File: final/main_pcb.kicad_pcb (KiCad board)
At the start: 2 copper layers, 136.8 x 105.5 mm, 93 parts

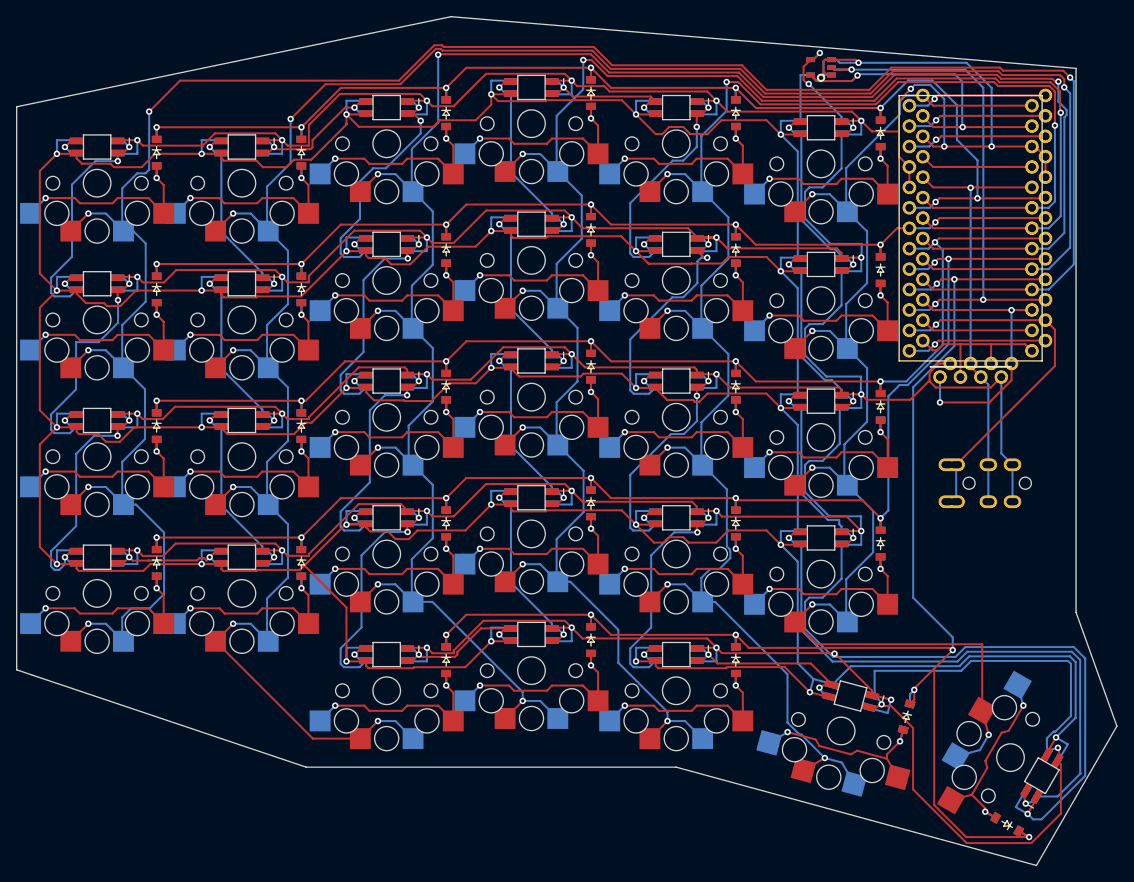
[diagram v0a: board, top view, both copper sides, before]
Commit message: Fix outline to have 0.3mm gap to traces
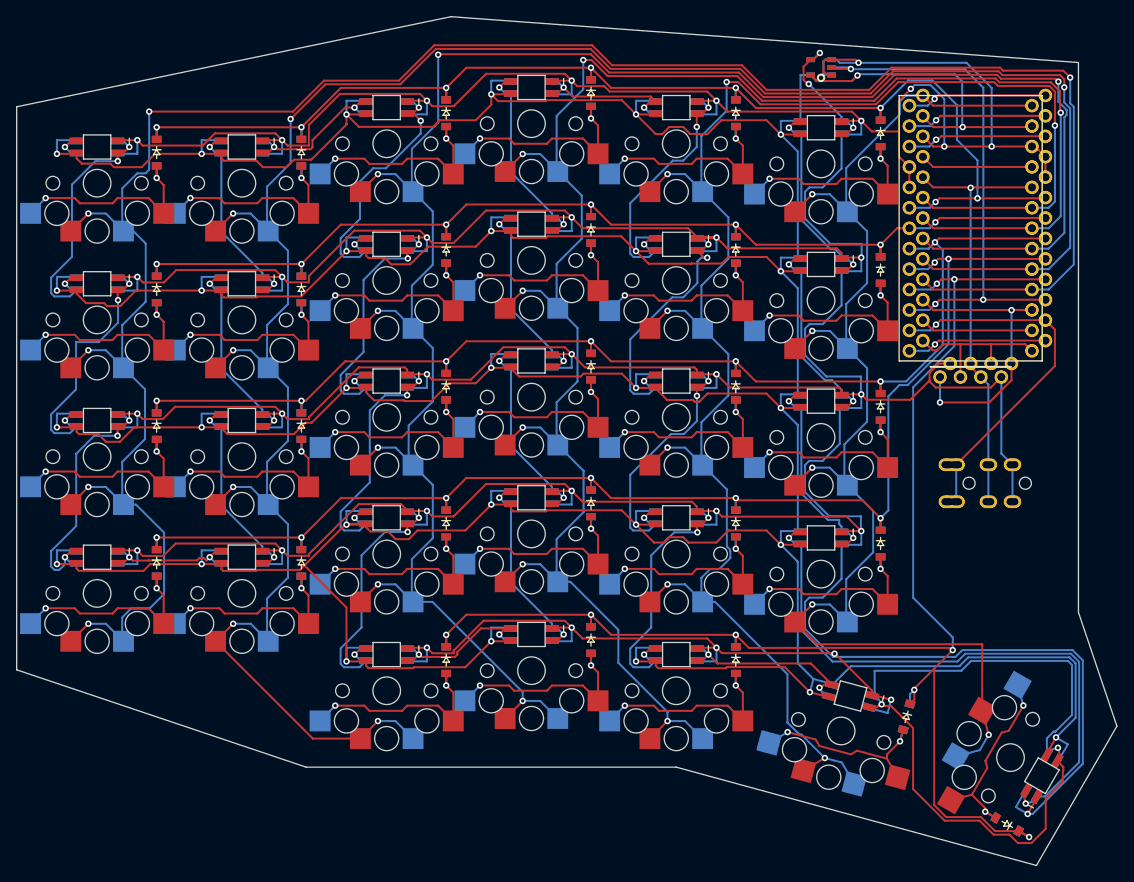
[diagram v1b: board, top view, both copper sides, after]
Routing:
- net RAW: track 837.6 -> 781.1 mm
- net GND: track 912.0 -> 909.6 mm
- net RMod: track 186.8 -> 185.2 mm
- net LED_4: track 75.8 -> 74.3 mm
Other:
- outline, holes or cut-outs redrawn

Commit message: Add picture footprnts and add to PCB Fix TRRS Power line on kicadpcb to 5v Add Readme on changes made
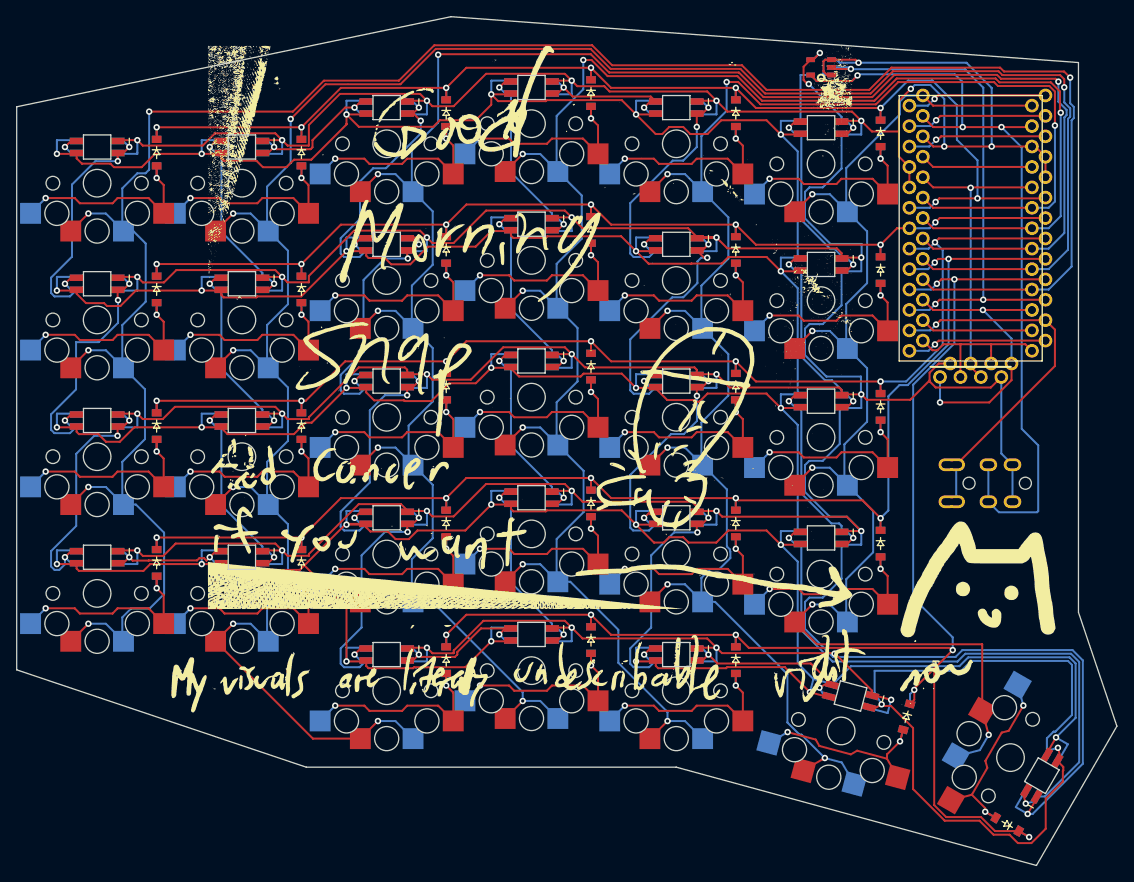
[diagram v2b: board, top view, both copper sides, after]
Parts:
- added  : LOGO, v7:plantjohnny_100, F.Cu at (191.8, 165.8)
- added G***: LOGO, v7:snap_80, F.Cu at (203.8, 149.9)
- added G***: LOGO, v7:visualsText, F.Cu at (209.0, 192.6)
- added G***: LOGO, v7:cat_20, F.Cu at (259.6, 181.1)
- added G***: LOGO, v7:rainbow_30, B.Cu at (234.2, 196.6)
- added G***: LOGO, v7:cat_20, B.Cu at (261.7, 180.6)
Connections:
- TRRS1 pad 3: 3V3 -> RAW
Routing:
- net RAW: track 781.1 -> 842.1 mm, vias 31 -> 32
- net 3V3: track 54.0 -> 38.1 mm
- net OLED_SDA: track 36.0 -> 37.5 mm
- net GND: track 909.6 -> 908.5 mm
